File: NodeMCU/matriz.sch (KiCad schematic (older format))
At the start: 11 parts, among them Q1 Q_NPN_BCE, U3 NodeMCU1.0(ESP-12E), U4 interfOut

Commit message: Actualizacion diseño FINAL con santi
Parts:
- added JP1, JP2, JP3, JP4: Jp_open_small, symbol Jumper_NO_Small
- added SW1: SW_Push_Open, symbol SW_Push_Open
- gave numbers to parts that had none: 6
- renumbered R2 to R1, R3 to R2
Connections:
- wire segments 38 -> 55
- no-connect marks 26 -> 23
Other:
- moved on the sheet: U3
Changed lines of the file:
@@
 L NodeMCU1.0(ESP-12E) U3
 U 1 1 59FF8FB1
-P 5800 4900
-F 0 "U3" H 5800 5750 60  0000 C CNN
-F 1 "NodeMCU1.0(ESP-12E)" H 5800 4050 60  0000 C CNN
-F 2 "" H 5200 4050 60  0000 C CNN
-F 3 "" H 5200 4050 60  0000 C CNN
-	1    5800 4900
-	1    0    0    -1
-$EndComp
-NoConn ~ 6600 4600
-NoConn ~ 6600 4700
-NoConn ~ 6600 4800
-NoConn ~ 6600 4900
-NoConn ~ 6600 5000
-NoConn ~ 6600 5100
-NoConn ~ 6600 5200
-NoConn ~ 6600 4200
-NoConn ~ 5000 4200
-NoConn ~ 5000 4300
-NoConn ~ 5000 4400
-NoConn ~ 5000 4500
-NoConn ~ 5000 4600
-NoConn ~ 5000 4700
-NoConn ~ 5000 4800
-NoConn ~ 5000 5000
-NoConn ~ 5000 5200
-NoConn ~ 5000 5300
-NoConn ~ 5000 5400
-NoConn ~ 6600 5300
-NoConn ~ 6600 5400
-NoConn ~ 6600 5500
-NoConn ~ 6600 5600
-NoConn ~ 5000 5500
-NoConn ~ 5000 5100
-$Comp
-L +5V #PWR02
-U 1 1 5A00823B
-P 7050 5950
-F 0 "#PWR02" H 7050 5800 50  0001 C CNN
-F 1 "+5V" H 7050 6090 50  0000 C CNN
-F 2 "" H 7050 5950 50  0001 C CNN
-F 3 "" H 7050 5950 50  0001 C CNN
-	1    7050 5950
-	1    0    0    -1
-$EndComp
+P 4950 4900
+F 0 "U3" H 4950 5750 60  0000 C CNN
+F 1 "NodeMCU1.0(ESP-12E)" H 4950 4050 60  0000 C CNN
+F 2 "" H 4350 4050 60  0000 C CNN
+F 3 "" H 4350 4050 60  0000 C CNN
+	1    4950 4900
+	1    0    0    -1
+$EndComp
+NoConn ~ 5750 4600
+NoConn ~ 5750 4700
+NoConn ~ 5750 4800
+NoConn ~ 4150 4200
+NoConn ~ 4150 4300
+NoConn ~ 4150 4400
+NoConn ~ 4150 4600
+NoConn ~ 4150 4700
+NoConn ~ 4150 4800
+NoConn ~ 4150 5000
+NoConn ~ 4150 5200
+NoConn ~ 4150 5300
+NoConn ~ 4150 5400
+NoConn ~ 5750 5300
+NoConn ~ 5750 5400
+NoConn ~ 5750 5500
+NoConn ~ 5750 5600
+NoConn ~ 4150 5500
+NoConn ~ 4150 5100
 $Comp
 L interfOut U4
@@
 	1    0    0    -1
 $EndComp
-NoConn ~ 5000 4900
+NoConn ~ 4150 4900
 $Comp
 L Q_NPN_BCE Q1
@@
 $EndComp
 $Comp
-L R R3
+L R R2
 U 1 1 5A048139
 P 8100 4800
-F 0 "R3" V 8180 4800 50  0000 C CNN
+F 0 "R2" V 8180 4800 50  0000 C CNN
 F 1 "0.7KOhm" V 8250 4800 50  0000 C CNN
 F 2 "" V 8030 4800 50  0001 C CNN
@@
 $EndComp
 $Comp
-L R R2
+L R R1
 U 1 1 5A048190
 P 7300 5200
-F 0 "R2" V 7400 5200 50  0000 C CNN
+F 0 "R1" V 7400 5200 50  0000 C CNN
 F 1 "50KOhm" V 7500 5200 50  0000 C CNN
 F 2 "" V 7230 5200 50  0001 C CNN
@@
 $EndComp
 $Comp
-L GND #PWR?
+L GND #PWR01
 U 1 1 5A04E6F4
-P 7750 5850
-F 0 "#PWR?" H 7750 5600 50  0001 C CNN
-F 1 "GND" H 7750 5700 50  0000 C CNN
-F 2 "" H 7750 5850 50  0001 C CNN
-F 3 "" H 7750 5850 50  0001 C CNN
-	1    7750 5850
-	1    0    0    -1
-$EndComp
-$Comp
-L Q_NPN_BCE Q?
+P 7750 6100
+F 0 "#PWR01" H 7750 5850 50  0001 C CNN
+F 1 "GND" H 7750 5950 50  0000 C CNN
+F 2 "" H 7750 6100 50  0001 C CNN
+F 3 "" H 7750 6100 50  0001 C CNN
+	1    7750 6100
+	1    0    0    -1
+$EndComp
+$Comp
+L Q_NPN_BCE Q2
 U 1 1 5A04F6F4
 P 8450 4400
-F 0 "Q?" H 8650 4450 50  0000 L CNN
+F 0 "Q2" H 8650 4450 50  0000 L CNN
 F 1 "Q_NPN_BCE" H 8650 4350 50  0000 L CNN
 F 2 "" H 8650 4500 50  0001 C CNN
@@
 $EndComp
 $Comp
-L R R?
+L R R4
 U 1 1 5A04F6FA
 P 8900 4000
-F 0 "R?" V 8980 4000 50  0000 C CNN
+F 0 "R4" V 8980 4000 50  0000 C CNN
 F 1 "0.7KOhm" V 9050 4000 50  0000 C CNN
 F 2 "" V 8830 4000 50  0001 C CNN
@@
 $EndComp
 $Comp
-L R R?
+L R R3
 U 1 1 5A04F700
 P 8100 4400
-F 0 "R?" V 8200 4400 50  0000 C CNN
+F 0 "R3" V 8200 4400 50  0000 C CNN
 F 1 "50KOhm" V 8300 4400 50  0000 C CNN
 F 2 "" V 8030 4400 50  0001 C CNN
@@
 $EndComp
 $Comp
-L Q_NPN_BCE Q?
+L Q_NPN_BCE Q3
 U 1 1 5A04F8C6
 P 7350 3900
-F 0 "Q?" H 7550 3950 50  0000 L CNN
+F 0 "Q3" H 7550 3950 50  0000 L CNN
 F 1 "Q_NPN_BCE" H 7550 3850 50  0000 L CNN
 F 2 "" H 7550 4000 50  0001 C CNN
@@
 $EndComp
 $Comp
-L R R?
+L R R6
 U 1 1 5A04F8CC
 P 7800 3500
-F 0 "R?" V 7880 3500 50  0000 C CNN
+F 0 "R6" V 7880 3500 50  0000 C CNN
 F 1 "0.7KOhm" V 7950 3500 50  0000 C CNN
 F 2 "" V 7730 3500 50  0001 C CNN
@@
 $EndComp
 $Comp
-L R R?
+L R R5
 U 1 1 5A04F8D2
 P 7000 3900
-F 0 "R?" V 7100 3900 50  0000 C CNN
+F 0 "R5" V 7100 3900 50  0000 C CNN
 F 1 "50KOhm" V 7200 3900 50  0000 C CNN
 F 2 "" V 6930 3900 50  0001 C CNN
@@
 	0    1    1    0
 $EndComp
-Wire Wire Line
-	6600 4300 6800 4300
-Wire Wire Line
-	6600 4500 6950 4500
-Wire Wire Line
-	7750 5400 7750 5850
+$Comp
+L SW_Push_Open SW1
+U 1 1 5A08CE04
+P 3700 5250
+F 0 "SW1" H 3700 5350 50  0000 C CNN
+F 1 "SW_Push_Open" H 3700 5175 50  0000 C CNN
+F 2 "" H 3700 5450 50  0001 C CNN
+F 3 "" H 3700 5450 50  0001 C CNN
+	1    3700 5250
+	0    1    1    0
+$EndComp
+$Comp
+L Jumper_NO_Small JP4
+U 1 1 5A08DDBF
+P 6800 5500
+F 0 "JP4" H 6800 5580 50  0000 C CNN
+F 1 "Jp_open_small" H 6810 5440 50  0000 C CNN
+F 2 "" H 6800 5500 50  0001 C CNN
+F 3 "" H 6800 5500 50  0001 C CNN
+	1    6800 5500
+	0    1    1    0
+$EndComp
+$Comp
+L Jumper_NO_Small JP3
+U 1 1 5A08DF42
+P 6550 5500
+F 0 "JP3" H 6550 5580 50  0000 C CNN
+F 1 "Jp_open_small" H 6560 5440 50  0000 C CNN
+F 2 "" H 6550 5500 50  0001 C CNN
+F 3 "" H 6550 5500 50  0001 C CNN
+	1    6550 5500
+	0    1    1    0
+$EndComp
+$Comp
+L Jumper_NO_Small JP2
+U 1 1 5A08DF95
+P 6300 5500
+F 0 "JP2" H 6300 5580 50  0000 C CNN
+F 1 "Jp_open_small" H 6310 5440 50  0000 C CNN
+F 2 "" H 6300 5500 50  0001 C CNN
+F 3 "" H 6300 5500 50  0001 C CNN
+	1    6300 5500
+	0    1    1    0
+$EndComp
+NoConn ~ 5750 4200
+NoConn ~ 4150 5600
+$Comp
+L Jumper_NO_Small JP1
+U 1 1 5A08EAB2
+P 4950 6050
+F 0 "JP1" H 4950 6130 50  0000 C CNN
+F 1 "Jp_open_small" H 4960 5990 50  0000 C CNN
+F 2 "" H 4950 6050 50  0001 C CNN
+F 3 "" H 4950 6050 50  0001 C CNN
+	1    4950 6050
+	-1   0    0    1
+$EndComp
+Wire Wire Line
+	5750 4300 6800 4300
+Wire Wire Line
+	5750 4500 6950 4500
+Wire Wire Line
+	7750 5400 7750 6100
 Wire Wire Line
 	7150 5200 6950 5200
@@
 	6950 5200 6950 4500
 Wire Wire Line
-	6600 4400 7950 4400
-Wire Wire Line
 	7950 4800 7750 4800
 Wire Wire Line
@@
 	8550 3150 8550 4200
 Wire Wire Line
-	7050 5950 7050 6150
-Wire Wire Line
-	9550 6150 4850 6150
-Wire Wire Line
-	4850 6150 4850 5600
-Wire Wire Line
-	4850 5600 5000 5600
+	3700 4850 3700 5050
 Wire Wire Line
 	7050 5600 9650 5600
@@
 	8250 4800 9550 4800
 Wire Wire Line
-	9550 3500 9550 6150
-Connection ~ 7050 6150
+	9550 3500 9550 6400
 Wire Wire Line
 	7650 3500 7450 3500
@@
 	8450 2750 8650 2750
 Connection ~ 8550 5600
+Wire Wire Line
+	3700 5450 3700 6400
+Wire Wire Line
+	6800 5600 6800 5750
+Wire Wire Line
+	6800 5750 7750 5750
+Connection ~ 7750 5750
+Wire Wire Line
+	6550 5600 6550 5850
+Wire Wire Line
+	6550 5850 7750 5850
+Connection ~ 7750 5850
+Wire Wire Line
+	6300 5600 6300 5950
+Wire Wire Line
+	6300 5950 7750 5950
+Wire Wire Line
+	5750 4900 6800 4900
+Wire Wire Line
+	5750 5000 6550 5000
+Wire Wire Line
+	5750 5100 6300 5100
+Wire Wire Line
+	7950 4400 5750 4400
+Wire Wire Line
+	5050 6050 7750 6050
+Connection ~ 7750 5950
+Wire Wire Line
+	6800 4900 6800 5400
+Wire Wire Line
+	6300 5100 6300 5400
+Wire Wire Line
+	6550 5000 6550 5400
+$Comp
+L +5V #PWR02
+U 1 1 5A00823B
+P 3700 4850
+F 0 "#PWR02" H 3700 4700 50  0001 C CNN
+F 1 "+5V" H 3700 4990 50  0000 C CNN
+F 2 "" H 3700 4850 50  0001 C CNN
+F 3 "" H 3700 4850 50  0001 C CNN
+	1    3700 4850
+	1    0    0    -1
+$EndComp
+$Comp
+L PWR_FLAG #FLG03
+U 1 1 5A090401
+P 3400 4850
+F 0 "#FLG03" H 3400 4925 50  0001 C CNN
+F 1 "PWR_FLAG" H 3400 5000 50  0000 C CNN
+F 2 "" H 3400 4850 50  0001 C CNN
+F 3 "" H 3400 4850 50  0001 C CNN
+	1    3400 4850
+	1    0    0    -1
+$EndComp
+Wire Wire Line
+	3700 4950 3400 4950
+Wire Wire Line
+	3400 4950 3400 4850
+Connection ~ 3700 4950
+Wire Wire Line
+	4150 4500 4050 4500
+Wire Wire Line
+	4050 4500 4050 6050
+Wire Wire Line
+	4050 6050 4850 6050
+NoConn ~ 5750 5200
+Connection ~ 7750 6050
+Wire Wire Line
+	3700 6400 9550 6400
 $EndSCHEMATC

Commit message: Esquematico testeado
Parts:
- removed U4: interfOut, symbol interfOut
- added J1: Conn_01x05, symbol Conn_01x05
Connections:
- net labels added: CLK, DOUT, GNDPWR, LD, V+
- wire segments 55 -> 59
- no-connect marks 23 -> 22
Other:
- moved on the sheet: Q1, R1, R2, SW1

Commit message: Footprint slave
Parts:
- added SW2: SW_Push, symbol SW_Push
- J1: footprint (none) -> Pin_Headers:Pin_Header_Angled_1x05_Pitch2.54mm
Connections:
- net GNDPWR: now also SW2.1
- net at U3.26 (D4(GPIO2)): now also SW2.2
- no-connect marks 22 -> 21
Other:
- moved on the sheet: JP2, JP3, JP4
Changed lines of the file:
@@
 F 0 "U3" H 4950 5750 60  0000 C CNN
 F 1 "NodeMCU1.0(ESP-12E)" H 4950 4050 60  0000 C CNN
-F 2 "" H 4350 4050 60  0000 C CNN
+F 2 "" H 4350 4050 60  0001 C CNN
 F 3 "" H 4350 4050 60  0000 C CNN
 	1    4950 4900
 	1    0    0    -1
 $EndComp
-NoConn ~ 5750 4600
 NoConn ~ 5750 4700
 NoConn ~ 5750 4800
@@
 L Jumper_NO_Small JP4
 U 1 1 5A08DDBF
-P 6800 5500
-F 0 "JP4" H 6800 5580 50  0000 C CNN
-F 1 "Jp_open_small" H 6810 5440 50  0000 C CNN
-F 2 "" H 6800 5500 50  0001 C CNN
-F 3 "" H 6800 5500 50  0001 C CNN
-	1    6800 5500
+P 6600 5500
+F 0 "JP4" H 6600 5580 50  0000 C CNN
+F 1 "Jp_open_small" H 6610 5440 50  0000 C CNN
+F 2 "" H 6600 5500 50  0001 C CNN
+F 3 "" H 6600 5500 50  0001 C CNN
+	1    6600 5500
 	0    1    1    0
 $EndComp
@@
 L Jumper_NO_Small JP3
 U 1 1 5A08DF42
-P 6550 5500
-F 0 "JP3" H 6550 5580 50  0000 C CNN
-F 1 "Jp_open_small" H 6560 5440 50  0000 C CNN
-F 2 "" H 6550 5500 50  0001 C CNN
-F 3 "" H 6550 5500 50  0001 C CNN
-	1    6550 5500
+P 6350 5500
+F 0 "JP3" H 6350 5580 50  0000 C CNN
+F 1 "Jp_open_small" H 6360 5440 50  0000 C CNN
+F 2 "" H 6350 5500 50  0001 C CNN
+F 3 "" H 6350 5500 50  0001 C CNN
+	1    6350 5500
 	0    1    1    0
 $EndComp
@@
 L Jumper_NO_Small JP2
 U 1 1 5A08DF95
-P 6300 5500
-F 0 "JP2" H 6300 5580 50  0000 C CNN
-F 1 "Jp_open_small" H 6310 5440 50  0000 C CNN
-F 2 "" H 6300 5500 50  0001 C CNN
-F 3 "" H 6300 5500 50  0001 C CNN
-	1    6300 5500
+P 6100 5500
+F 0 "JP2" H 6100 5580 50  0000 C CNN
+F 1 "Jp_open_small" H 6110 5440 50  0000 C CNN
+F 2 "" H 6100 5500 50  0001 C CNN
+F 3 "" H 6100 5500 50  0001 C CNN
+	1    6100 5500
 	0    1    1    0
 $EndComp
@@
 F 0 "J1" H 9050 3250 50  0000 C CNN
 F 1 "Conn_01x05" H 9050 2650 50  0000 C CNN
-F 2 "" H 9050 2950 50  0001 C CNN
+F 2 "Pin_Headers:Pin_Header_Angled_1x05_Pitch2.54mm" H 9050 2950 50  0001 C CNN
 F 3 "" H 9050 2950 50  0001 C CNN
 	1    9050 2950
@@
 	7250 2950 8850 2950
 Wire Wire Line
-	9650 2500 9650 5600
+	9650 5600 9650 2500
 Wire Wire Line
 	9650 2500 8350 2500
@@
 	8350 2750 8850 2750
 Wire Wire Line
-	6800 5600 6800 5750
-Wire Wire Line
-	6550 5600 6550 5850
-Wire Wire Line
-	6300 5600 6300 5950
-Wire Wire Line
-	5750 4900 6800 4900
-Wire Wire Line
-	5750 5000 6550 5000
-Wire Wire Line
-	5750 5100 6300 5100
-Wire Wire Line
-	6800 4900 6800 5400
-Wire Wire Line
-	6300 5100 6300 5400
-Wire Wire Line
-	6550 5000 6550 5400
+	6600 5600 6600 5750
+Wire Wire Line
+	6350 5600 6350 5850
+Wire Wire Line
+	6100 5600 6100 5950
+Wire Wire Line
+	6600 4900 6600 5400
+Wire Wire Line
+	6100 5100 6100 5400
+Wire Wire Line
+	6350 5000 6350 5400
 Wire Wire Line
 	3800 2750 3500 2750
@@
 	7550 5300 7550 6200
 Wire Wire Line
-	6300 5950 7550 5950
+	6100 5950 7550 5950
 Connection ~ 7550 5950
 Wire Wire Line
-	6550 5850 7550 5850
-Wire Wire Line
-	6800 5750 7550 5750
+	6350 5850 7550 5850
+Wire Wire Line
+	6600 5750 7550 5750
 Connection ~ 7550 5850
 Connection ~ 7550 5750
@@
 Connection ~ 7250 3250
 Wire Wire Line
-	9650 5600 7550 5600
+	6850 5600 9650 5600
 Connection ~ 7550 5600
 Wire Wire Line
@@
 Wire Wire Line
 	3800 5600 3800 3250
+Wire Wire Line
+	6600 4900 5750 4900
+Wire Wire Line
+	6350 5000 5750 5000
+Wire Wire Line
+	6100 5100 5750 5100
+$Comp
+L SW_Push SW2
+U 1 1 5A121D29
+P 6850 5400
+F 0 "SW2" H 6900 5500 50  0000 L CNN
+F 1 "SW_Push" H 6850 5340 50  0000 C CNN
+F 2 "" H 6850 5600 50  0001 C CNN
+F 3 "" H 6850 5600 50  0001 C CNN
+	1    6850 5400
+	0    -1   -1   0
+$EndComp
+Wire Wire Line
+	5750 4600 5950 4600
+Wire Wire Line
+	5950 4600 5950 4800
+Wire Wire Line
+	5950 4800 6850 4800
+Wire Wire Line
+	6850 4800 6850 5200
 $EndSCHEMATC

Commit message: master changes
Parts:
- JP1, JP2, JP3, JP4, SW1, SW2: footprint (none) -> Connectors:PINHEAD1-2
- Q1, Q2, Q3: footprint (none) -> Transistors_OldSowjetAera:OldSowjetaera_Transistor_Type-II_BigPads
- R1, R2, R3, R4, R5, R6: footprint (none) -> Resistors_THT:R_Axial_DIN0207_L6.3mm_D2.5mm_P7.62mm_Horizontal
- U3: footprint (none) -> NodeMCU:NodeMCU1.0(12-E)
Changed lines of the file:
@@
 F 0 "U3" H 4950 5750 60  0000 C CNN
 F 1 "NodeMCU1.0(ESP-12E)" H 4950 4050 60  0000 C CNN
-F 2 "" H 4350 4050 60  0001 C CNN
+F 2 "NodeMCU:NodeMCU1.0(12-E)" H 4350 4050 60  0001 C CNN
 F 3 "" H 4350 4050 60  0000 C CNN
 	1    4950 4900
@@
 F 0 "SW1" H 3800 3150 50  0000 C CNN
 F 1 "SW_Push_Open" H 3800 2975 50  0000 C CNN
-F 2 "" H 3800 3250 50  0001 C CNN
+F 2 "Connectors:PINHEAD1-2" H 3800 3250 50  0001 C CNN
 F 3 "" H 3800 3250 50  0001 C CNN
 	1    3800 3050
@@
 F 0 "JP4" H 6600 5580 50  0000 C CNN
 F 1 "Jp_open_small" H 6610 5440 50  0000 C CNN
-F 2 "" H 6600 5500 50  0001 C CNN
+F 2 "Connectors:PINHEAD1-2" H 6600 5500 50  0001 C CNN
 F 3 "" H 6600 5500 50  0001 C CNN
 	1    6600 5500
@@
 F 0 "JP3" H 6350 5580 50  0000 C CNN
 F 1 "Jp_open_small" H 6360 5440 50  0000 C CNN
-F 2 "" H 6350 5500 50  0001 C CNN
+F 2 "Connectors:PINHEAD1-2" H 6350 5500 50  0001 C CNN
 F 3 "" H 6350 5500 50  0001 C CNN
 	1    6350 5500
@@
 F 0 "JP2" H 6100 5580 50  0000 C CNN
 F 1 "Jp_open_small" H 6110 5440 50  0000 C CNN
-F 2 "" H 6100 5500 50  0001 C CNN
+F 2 "Connectors:PINHEAD1-2" H 6100 5500 50  0001 C CNN
 F 3 "" H 6100 5500 50  0001 C CNN
 	1    6100 5500
@@
 F 0 "JP1" H 4950 6130 50  0000 C CNN
 F 1 "Jp_open_small" H 4960 5990 50  0000 C CNN
-F 2 "" H 4950 6050 50  0001 C CNN
+F 2 "Connectors:PINHEAD1-2" H 4950 6050 50  0001 C CNN
 F 3 "" H 4950 6050 50  0001 C CNN
 	1    4950 6050
@@
 F 0 "R1" V 7200 4700 50  0000 C CNN
 F 1 "50KOhm" V 7300 4700 50  0000 C CNN
-F 2 "" V 7030 4700 50  0001 C CNN
+F 2 "Resistors_THT:R_Axial_DIN0207_L6.3mm_D2.5mm_P7.62mm_Horizontal" V 7030 4700 50  0001 C CNN
 F 3 "" H 7100 4700 50  0001 C CNN
 	1    7100 4700
@@
 F 0 "R2" V 7630 5150 50  0000 C CNN
 F 1 "0.7KOhm" V 7700 5150 50  0000 C CNN
-F 2 "" V 7480 5150 50  0001 C CNN
+F 2 "Resistors_THT:R_Axial_DIN0207_L6.3mm_D2.5mm_P7.62mm_Horizontal" V 7480 5150 50  0001 C CNN
 F 3 "" H 7550 5150 50  0001 C CNN
 	1    7550 5150
@@
 F 0 "Q1" H 7650 4750 50  0000 L CNN
 F 1 "Q_NPN_BCE" H 7650 4650 50  0000 L CNN
-F 2 "" H 7650 4800 50  0001 C CNN
+F 2 "Transistors_OldSowjetAera:OldSowjetaera_Transistor_Type-II_BigPads" H 7650 4800 50  0001 C CNN
 F 3 "" H 7450 4700 50  0001 C CNN
 	1    7450 4700
@@
 F 0 "R3" V 8500 4400 50  0000 C CNN
 F 1 "50KOhm" V 8600 4400 50  0000 C CNN
-F 2 "" V 8330 4400 50  0001 C CNN
+F 2 "Resistors_THT:R_Axial_DIN0207_L6.3mm_D2.5mm_P7.62mm_Horizontal" V 8330 4400 50  0001 C CNN
 F 3 "" H 8400 4400 50  0001 C CNN
 	1    8400 4400
@@
 F 0 "R4" V 8930 4850 50  0000 C CNN
 F 1 "0.7KOhm" V 9000 4850 50  0000 C CNN
-F 2 "" V 8780 4850 50  0001 C CNN
+F 2 "Resistors_THT:R_Axial_DIN0207_L6.3mm_D2.5mm_P7.62mm_Horizontal" V 8780 4850 50  0001 C CNN
 F 3 "" H 8850 4850 50  0001 C CNN
 	1    8850 4850
@@
 F 0 "Q2" H 8950 4450 50  0000 L CNN
 F 1 "Q_NPN_BCE" H 8950 4350 50  0000 L CNN
-F 2 "" H 8950 4500 50  0001 C CNN
+F 2 "Transistors_OldSowjetAera:OldSowjetaera_Transistor_Type-II_BigPads" H 8950 4500 50  0001 C CNN
 F 3 "" H 8750 4400 50  0001 C CNN
 	1    8750 4400
@@
 F 0 "R5" V 6900 3500 50  0000 C CNN
 F 1 "50KOhm" V 7000 3500 50  0000 C CNN
-F 2 "" V 6730 3500 50  0001 C CNN
+F 2 "Resistors_THT:R_Axial_DIN0207_L6.3mm_D2.5mm_P7.62mm_Horizontal" V 6730 3500 50  0001 C CNN
 F 3 "" H 6800 3500 50  0001 C CNN
 	1    6800 3500
@@
 F 0 "R6" V 7330 3950 50  0000 C CNN
 F 1 "0.7KOhm" V 7400 3950 50  0000 C CNN
-F 2 "" V 7180 3950 50  0001 C CNN
+F 2 "Resistors_THT:R_Axial_DIN0207_L6.3mm_D2.5mm_P7.62mm_Horizontal" V 7180 3950 50  0001 C CNN
 F 3 "" H 7250 3950 50  0001 C CNN
 	1    7250 3950
@@
 F 0 "Q3" H 7350 3550 50  0000 L CNN
 F 1 "Q_NPN_BCE" H 7350 3450 50  0000 L CNN
-F 2 "" H 7350 3600 50  0001 C CNN
+F 2 "Transistors_OldSowjetAera:OldSowjetaera_Transistor_Type-II_BigPads" H 7350 3600 50  0001 C CNN
 F 3 "" H 7150 3500 50  0001 C CNN
 	1    7150 3500
@@
 F 0 "SW2" H 6900 5500 50  0000 L CNN
 F 1 "SW_Push" H 6850 5340 50  0000 C CNN
-F 2 "" H 6850 5600 50  0001 C CNN
+F 2 "Connectors:PINHEAD1-2" H 6850 5600 50  0001 C CNN
 F 3 "" H 6850 5600 50  0001 C CNN
 	1    6850 5400

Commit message: Cosas del dia 30 en barcara
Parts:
- removed Q1, Q2, Q3: Q_NPN_BCE, Transistors_OldSowjetAera:OldSowjetaera_Transistor_Type-II_BigPads, symbol Q_NPN_BCE
- added Q1, Q2, Q3: Q_NPN_CBE, Transistors_OldSowjetAera:OldSowjetaera_Transistor_Type-II_BigPads, symbol Q_NPN_CBE
- J1: footprint Pin_Headers:Pin_Header_Angled_1x05_Pitch2.54mm -> Pin_Headers:Pin_Header_Straight_1x05_Pitch2.54mm
- U3: footprint NodeMCU:NodeMCU1.0(12-E) -> ESP8266:NodeMCU1.0(12-E)
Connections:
- net CLK: now also R2.1, Q1.1 (C); no longer R2.2
- net DOUT: now also R6.1, Q3.1 (C); no longer R6.2
- net GNDPWR: now also Q1.3 (E), Q2.3 (E), Q3.3 (E); no longer R2.1, R4.1, R6.1
- net LD: now also R4.1, Q2.1 (C); no longer R4.2
- net V+: now also R2.2, R4.2, R6.2
- net at R1.1: now also Q1.2 (B)
- net at R3.1: now also Q2.2 (B)
- net at R5.1: now also Q3.2 (B)
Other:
- moved on the sheet: R1, R2, R3, R4, R5, R6

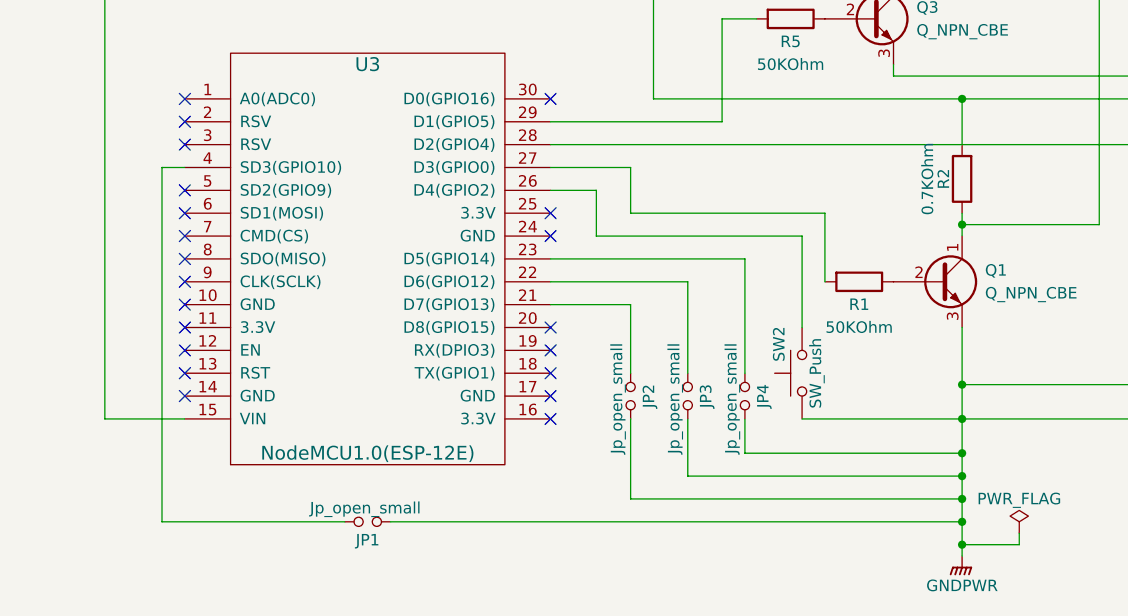
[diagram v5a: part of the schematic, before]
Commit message: Saco un jumprs y reacomodo
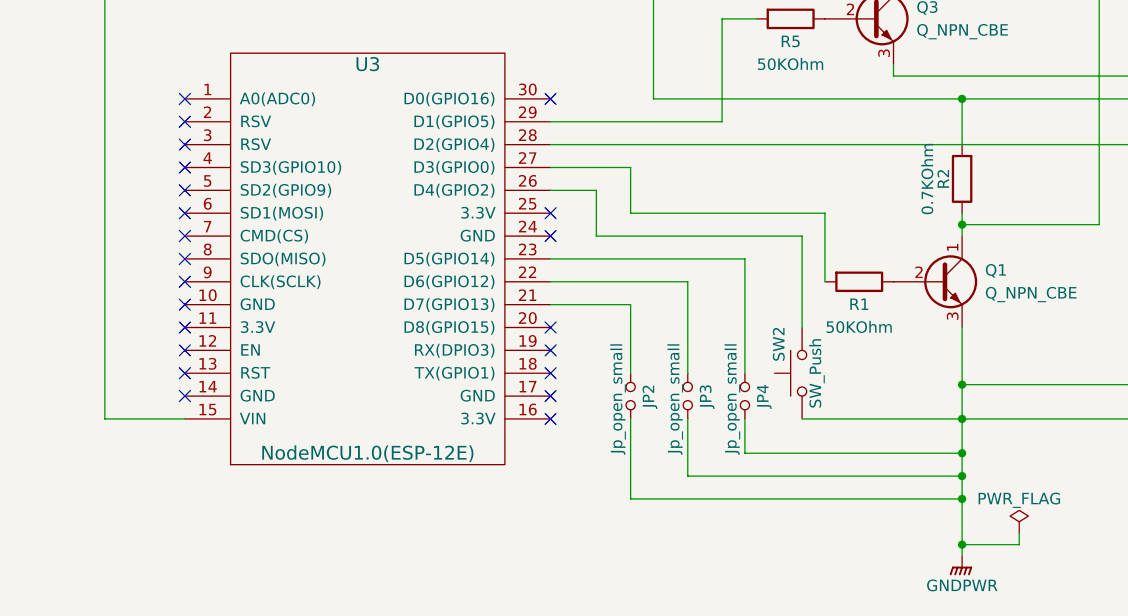
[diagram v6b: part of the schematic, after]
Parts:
- removed JP1: Jp_open_small, Connectors:PINHEAD1-2, symbol Jumper_NO_Small
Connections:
- no-connect marks 21 -> 22
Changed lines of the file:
@@
 NoConn ~ 5750 4200
-$Comp
-L Jumper_NO_Small JP1
-U 1 1 5A08EAB2
-P 4950 6050
-F 0 "JP1" H 4950 6130 50  0000 C CNN
-F 1 "Jp_open_small" H 4960 5990 50  0000 C CNN
-F 2 "Connectors:PINHEAD1-2" H 4950 6050 50  0001 C CNN
-F 3 "" H 4950 6050 50  0001 C CNN
-	1    4950 6050
-	-1   0    0    1
-$EndComp
 $Comp
 L +5V #PWR01
@@
 Connection ~ 3800 2750
 Wire Wire Line
-	4150 4500 4050 4500
-Wire Wire Line
-	4050 4500 4050 6050
-Wire Wire Line
-	4050 6050 4850 6050
-Wire Wire Line
 	8350 2500 8350 2750
 Wire Wire Line
@@
 Connection ~ 7550 5850
 Connection ~ 7550 5750
-Wire Wire Line
-	5050 6050 7550 6050
-Connection ~ 7550 6050
 Wire Wire Line
 	7550 6150 7800 6150
@@
 	1    0    0    -1
 $EndComp
+NoConn ~ 4150 4500
 $EndSCHEMATC
